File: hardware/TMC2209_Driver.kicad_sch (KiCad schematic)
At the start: 30 parts, among them J1 PCIe_Stepper, J2 Conn_01x04_Male, U1 TMC2209-LA, U2 74LVC1G06, U3 24LC02

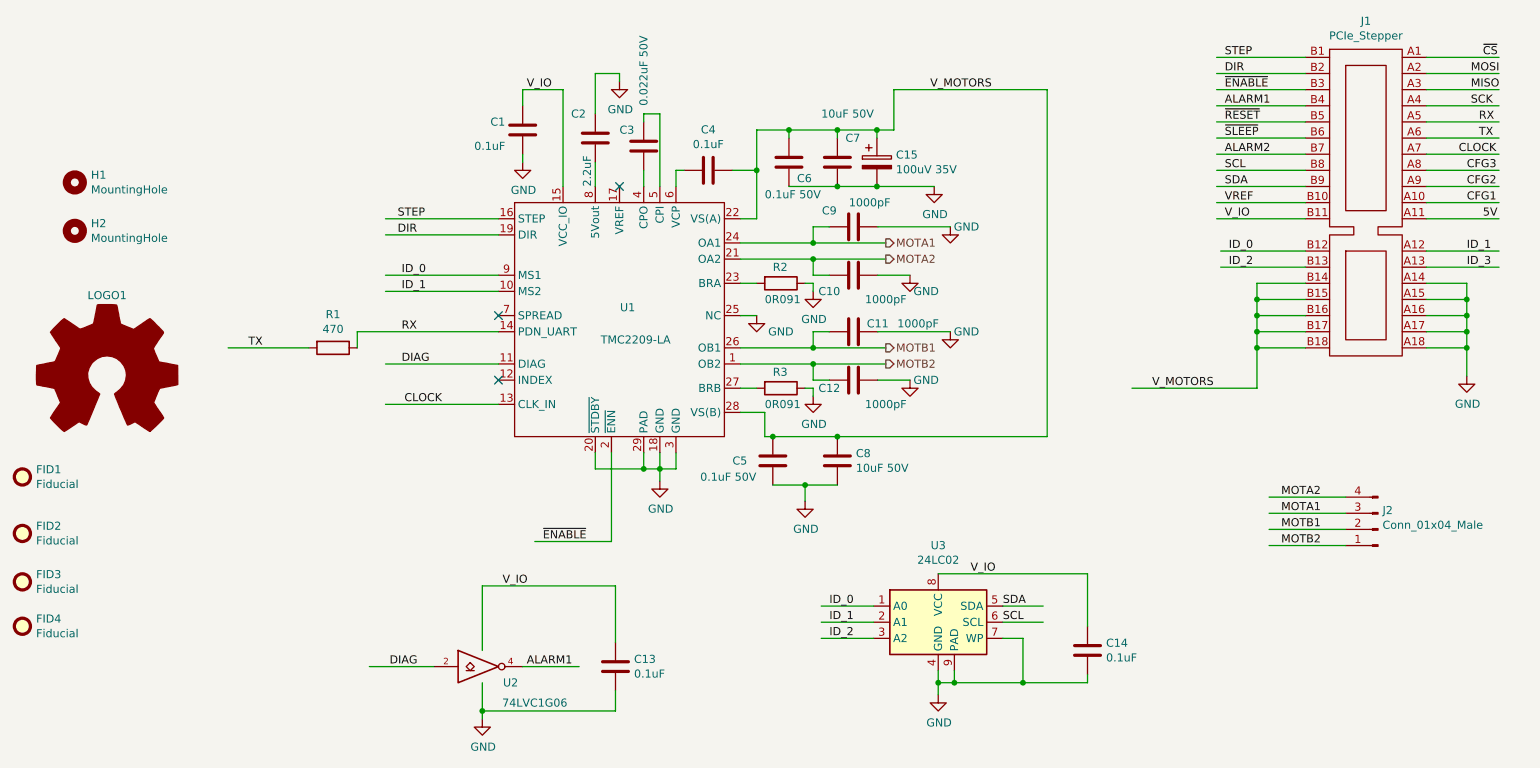
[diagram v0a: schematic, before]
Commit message: Added jumper for the TMC2209 driver clock selection.
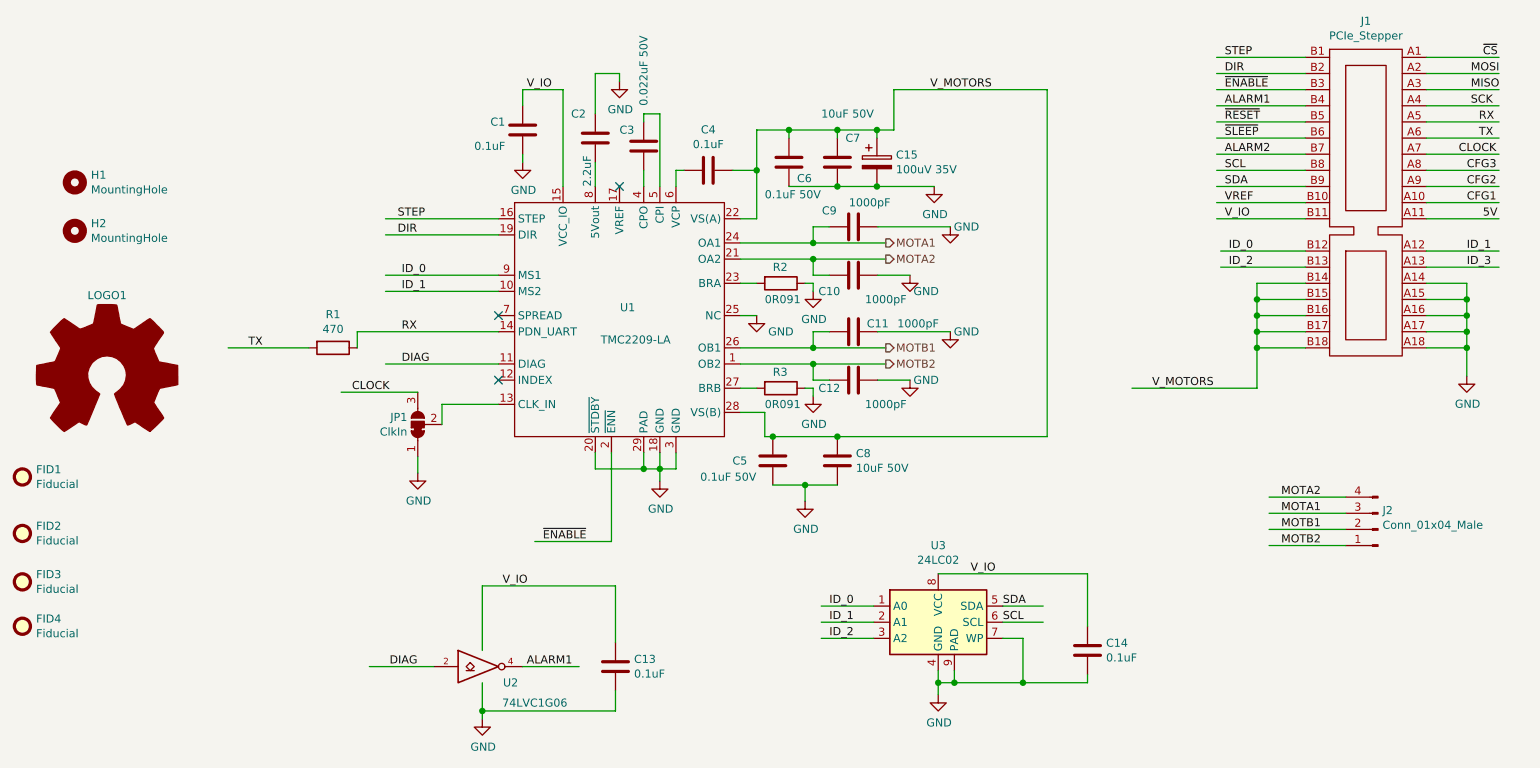
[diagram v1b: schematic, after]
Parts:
- added JP1: ClkIn, Jumper:SolderJumper-3_P1.3mm_Bridged12_Pad1.0x1.5mm, symbol Jumper:SolderJumper_3_Bridged12
- FID1, FID2, FID3, FID4, H1, H2, J1, LOGO1: now left out of the parts list
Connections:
- net CLOCK: now also JP1.3 (B); no longer U1.13 (CLK_IN)
- net GND: now also JP1.1 (A)
- new net: JP1.2 (C), U1.13 (CLK_IN)

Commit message: Convert SCH files to latest version. Fix DRC Warnings in PrntrBoard.
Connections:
- net ~CS renamed ~{CS}
- net ~ENABLE renamed ~{ENABLE}
- net ~RESET renamed ~{RESET}
- net ~SLEEP renamed ~{SLEEP}
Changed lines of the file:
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@@
-(kicad_sch (version 20201015) (generator eeschema)
+(kicad_sch (version 20210621) (generator eeschema)
   (paper "A4")
   (junction (at 99.06 151.13) (diameter 1.016) (color 0 0 0 0))
@@
   (junction (at 254 91.44) (diameter 1.016) (color 0 0 0 0))
   (junction (at 254 93.98) (diameter 1.016) (color 0 0 0 0))
+  (no_connect (at 101.6 88.9))
   (no_connect (at 101.6 99.06))
   (no_connect (at 120.65 68.58))
-  (no_connect (at 101.6 88.9))
   (wire (pts (xy 71.755 93.98) (xy 59.055 93.98))
     (stroke (width 0) (type solid) (color 0 0 0 0))
@@
     (effects (font (size 1.27 1.27)) (justify left bottom))
   )
-  (label "~ENABLE" (at 108.585 124.46 0)
+  (label "~{ENABLE}" (at 108.585 124.46 0)
     (effects (font (size 1.27 1.27)) (justify left bottom))
   )
@@
     (effects (font (size 1.27 1.27)) (justify left bottom))
   )
-  (label "~ENABLE" (at 215.9 53.34 0)
+  (label "~{ENABLE}" (at 215.9 53.34 0)
     (effects (font (size 1.27 1.27)) (justify left bottom))
   )
@@
     (effects (font (size 1.27 1.27)) (justify left bottom))
   )
-  (label "~RESET" (at 215.9 58.42 0)
-    (effects (font (size 1.27 1.27)) (justify left bottom))
-  )
-  (label "~SLEEP" (at 215.9 60.96 0)
+  (label "~{RESET}" (at 215.9 58.42 0)
+    (effects (font (size 1.27 1.27)) (justify left bottom))
+  )
+  (label "~{SLEEP}" (at 215.9 60.96 0)
     (effects (font (size 1.27 1.27)) (justify left bottom))
   )
@@
     (effects (font (size 1.27 1.27)) (justify left bottom))
   )
-  (label "~CS" (at 256.54 48.26 0)
+  (label "~{CS}" (at 256.54 48.26 0)
     (effects (font (size 1.27 1.27)) (justify left bottom))
   )
@@
       (effects (font (size 1.27 1.27)) hide)
     )
+    (pin "1")
   )
   (symbol (lib_id "power:GND") (at 99.06 152.4 0) (unit 1)
@@
       (effects (font (size 1.27 1.27)) hide)
     )
+    (pin "1")
   )
   (symbol (lib_id "power:GND") (at 105.41 64.77 0) (unit 1)
@@
       (effects (font (size 1.27 1.27)) hide)
     )
+    (pin "1")
   )
   (symbol (lib_id "power:GND") (at 120.65 52.07 0) (unit 1)
@@
       (effects (font (size 1.27 1.27)) hide)
     )
+    (pin "1")
   )
   (symbol (lib_id "power:GND") (at 127 114.935 0) (unit 1)
@@
       (effects (font (size 1.27 1.27)) hide)
     )
+    (pin "1")
   )
   (symbol (lib_id "power:GND") (at 142.24 88.9 0) (unit 1)
@@
       (effects (font (size 1.27 1.27)) hide)
     )
+    (pin "1")
   )
   (symbol (lib_id "power:GND") (at 149.86 118.11 0) (unit 1)
@@
       (effects (font (size 1.27 1.27)) hide)
     )
+    (pin "1")
   )
   (symbol (lib_id "power:GND") (at 151.13 85.09 0) (unit 1)
@@
       (effects (font (size 1.27 1.27)) hide)
     )
+    (pin "1")
   )
   (symbol (lib_id "power:GND") (at 151.13 101.6 0) (unit 1)
@@
       (effects (font (size 1.27 1.27)) hide)
     )
+    (pin "1")
   )
   (symbol (lib_id "power:GND") (at 166.37 82.55 0) (unit 1)
@@
       (effects (font (size 1.27 1.27)) hide)
     )
+    (pin "1")
   )
   (symbol (lib_id "power:GND") (at 166.37 99.06 0) (unit 1)
@@
       (effects (font (size 1.27 1.27)) hide)
     )
+    (pin "1")
   )
   (symbol (lib_id "power:GND") (at 170.18 68.58 0) (unit 1)
@@
       (effects (font (size 1.27 1.27)) hide)
     )
+    (pin "1")
   )
   (symbol (lib_id "power:GND") (at 170.815 148.59 0) (unit 1)
@@
       (effects (font (size 1.27 1.27)) hide)
     )
+    (pin "1")
   )
   (symbol (lib_id "power:GND") (at 172.72 74.93 0) (unit 1)
@@
       (effects (font (size 1.27 1.27)) hide)
     )
+    (pin "1")
   )
   (symbol (lib_id "power:GND") (at 172.72 91.44 0) (unit 1)
@@
       (effects (font (size 1.27 1.27)) hide)
     )
+    (pin "1")
   )
   (symbol (lib_id "power:GND") (at 254 98.425 0) (unit 1)
@@
       (effects (font (size 1.27 1.27)) hide)
     )
+    (pin "1")
   )
   (symbol (lib_id "Mechanical:Fiducial") (at 26.67 114.3 0) (unit 1)
@@
       (effects (font (size 1.27 1.27)) hide)
     )
+    (pin "1")
+    (pin "2")
   )
   (symbol (lib_id "Device:R") (at 146.05 83.82 270) (unit 1)
@@
       (effects (font (size 1.27 1.27)) hide)
     )
+    (pin "1")
+    (pin "2")
   )
   (symbol (lib_id "Device:R") (at 146.05 100.33 270) (unit 1)
@@
       (effects (font (size 1.27 1.27)) hide)
     )
+    (pin "1")
+    (pin "2")
   )
   (symbol (lib_id "Device:C") (at 105.41 59.69 0) (unit 1)
@@
       (effects (font (size 1.27 1.27)) hide)
     )
+    (pin "1")
+    (pin "2")
   )
   (symbol (lib_id "Device:C") (at 116.84 60.96 0) (unit 1)
@@
       (effects (font (size 1.27 1.27)) hide)
     )
+    (pin "1")
+    (pin "2")
   )
   (symbol (lib_id "Device:C") (at 120.015 144.145 0) (unit 1)
@@
       (effects (font (size 1.27 1.27)) hide)
     )
+    (pin "1")
+    (pin "2")
   )
   (symbol (lib_id "Device:C") (at 124.46 62.23 0) (unit 1)
@@
       (effects (font (size 1.27 1.27)) hide)
     )
+    (pin "1")
+    (pin "2")
   )
   (symbol (lib_id "Device:C") (at 134.62 66.04 270) (unit 1)
@@
       (effects (font (size 1.27 1.27)) hide)
     )
+    (pin "1")
+    (pin "2")
   )
   (symbol (lib_id "Device:C") (at 144.78 111.76 0) (unit 1)
@@
       (effects (font (size 1.27 1.27)) hide)
     )
+    (pin "1")
+    (pin "2")
   )
   (symbol (lib_id "Device:C") (at 147.32 64.77 0) (unit 1)
@@
       (effects (font (size 1.27 1.27)) hide)
     )
+    (pin "1")
+    (pin "2")
   )
   (symbol (lib_id "Device:C") (at 154.94 64.77 0) (unit 1)
@@
       (effects (font (size 1.27 1.27)) hide)
     )
+    (pin "1")
+    (pin "2")
   )
   (symbol (lib_id "Device:C") (at 154.94 111.76 0) (unit 1)
@@
       (effects (font (size 1.27 1.27)) hide)
     )
+    (pin "1")
+    (pin "2")
   )
   (symbol (lib_id "Device:C") (at 157.48 74.93 270) (unit 1)
@@
       (effects (font (size 1.27 1.27)) hide)
     )
+    (pin "1")
+    (pin "2")
   )
   (symbol (lib_id "Device:C") (at 157.48 82.55 270) (unit 1)
@@
       (effects (font (size 1.27 1.27)) hide)
     )
+    (pin "1")
+    (pin "2")
   )
   (symbol (lib_id "Device:C") (at 157.48 91.44 270) (unit 1)
@@
       (effects (font (size 1.27 1.27)) hide)
     )
+    (pin "1")
+    (pin "2")
   )
   (symbol (lib_id "Device:C") (at 157.48 99.06 270) (unit 1)
@@
       (effects (font (size 1.27 1.27)) hide)
     )
+    (pin "1")
+    (pin "2")
   )
   (symbol (lib_id "Device:CP") (at 161.163 64.77 0) (unit 1)
@@
       (effects (font (size 1.27 1.27)) hide)
     )
+    (pin "1")
+    (pin "2")
   )
   (symbol (lib_id "Device:C") (at 194.31 141.605 0) (unit 1)
@@
       (effects (font (size 1.27 1.27)) hide)
     )
+    (pin "1")
+    (pin "2")
   )
   (symbol (lib_id "Connector:Conn_01x04_Male") (at 240.03 122.555 180) (unit 1)
@@
       (effects (font (size 1.27 1.27)) hide)
     )
+    (pin "1")
+    (pin "2")
+    (pin "3")
+    (pin "4")
   )
   (symbol (lib_id "Jumper:SolderJumper_3_Bridged12") (at 88.9 106.045 90) (unit 1)
@@
       (effects (font (size 1.27 1.27)) hide)
     )
+    (pin "1")
+    (pin "2")
+    (pin "3")
   )
   (symbol (lib_id "Logic_74xgxx:74LVC1G06") (at 99.06 144.145 0) (unit 1)
@@
       (effects (font (size 1.27 1.27)) hide)
     )
+    (pin "2")
+    (pin "3")
+    (pin "4")
+    (pin "5")
   )
   (symbol (lib_id "24lc02:24LC02") (at 170.815 137.16 0) (unit 1)
@@
       (effects (font (size 1.27 1.27)) hide)
     )
+    (pin "1")
+    (pin "2")
+    (pin "3")
+    (pin "4")
+    (pin "5")
+    (pin "6")
+    (pin "7")
+    (pin "8")
+    (pin "9")
   )
   (symbol (lib_id "Graphic:Logo_Open_Hardware_Large") (at 40.005 98.425 0) (unit 1)
@@
       (effects (font (size 1.27 1.27)) hide)
     )
+    (pin "A1")
+    (pin "A10")
+    (pin "A11")
+    (pin "A12")
+    (pin "A13")
+    (pin "A14")
+    (pin "A15")
+    (pin "A16")
+    (pin "A17")
+    (pin "A18")
+    (pin "A2")
+    (pin "A3")
+    (pin "A4")
+    (pin "A5")
+    (pin "A6")
+    (pin "A7")
+    (pin "A8")
+    (pin "A9")
+    (pin "B1")
+    (pin "B10")
+    (pin "B11")
+    (pin "B12")
+    (pin "B13")
+    (pin "B14")
+    (pin "B15")
+    (pin "B16")
+    (pin "B17")
+    (pin "B18")
+    (pin "B2")
+    (pin "B3")
+    (pin "B4")
+    (pin "B5")
+    (pin "B6")
+    (pin "B7")
+    (pin "B8")
+    (pin "B9")
   )
   (symbol (lib_id "tmc2209:TMC2209-LA") (at 120.65 90.17 0) (unit 1)
@@
       (effects (font (size 1.27 1.27)) hide)
     )
+    (pin "1")
+    (pin "10")
+    (pin "11")
+    (pin "12")
+    (pin "13")
+    (pin "14")
+    (pin "15")
+    (pin "16")
+    (pin "17")
+    (pin "18")
+    (pin "19")
+    (pin "2")
+    (pin "20")
+    (pin "21")
+    (pin "22")
+    (pin "23")
+    (pin "24")
+    (pin "25")
+    (pin "26")
+    (pin "27")
+    (pin "28")
+    (pin "29")
+    (pin "3")
+    (pin "4")
+    (pin "5")
+    (pin "6")
+    (pin "7")
+    (pin "8")
+    (pin "9")
   )
   (sheet_instances

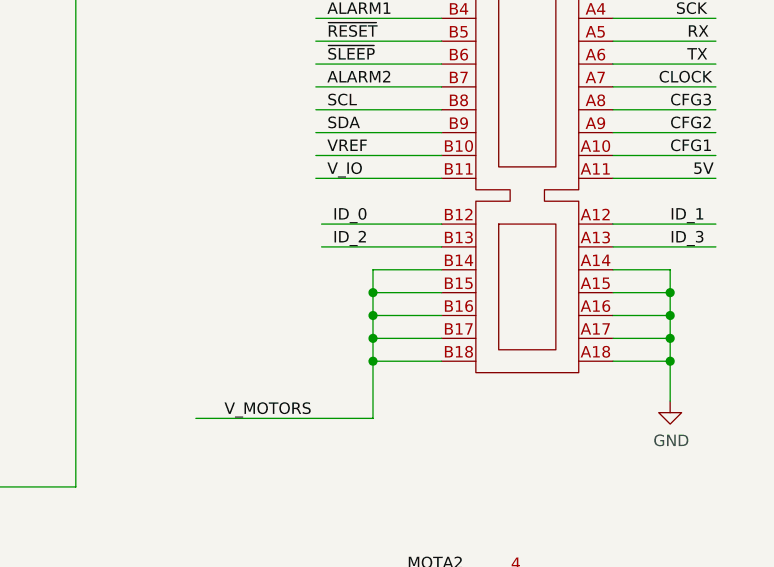
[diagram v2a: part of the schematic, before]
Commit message: Update drivers to respect high motor coltage circuit.
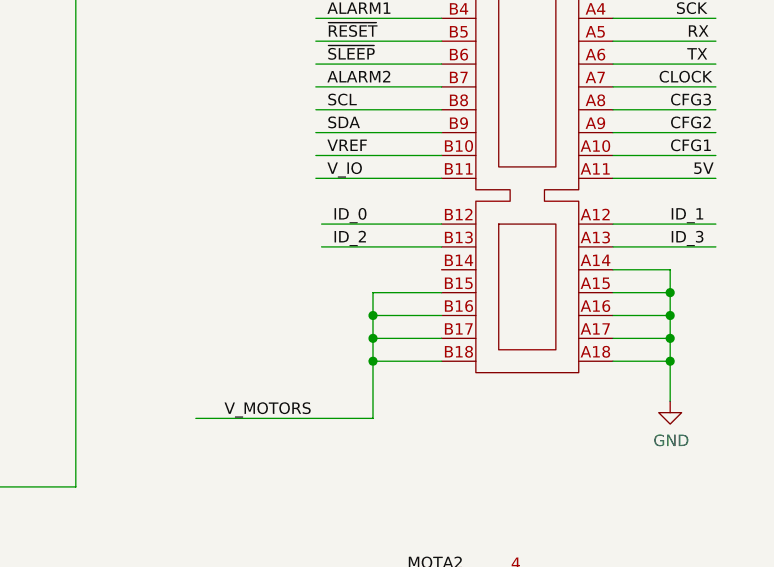
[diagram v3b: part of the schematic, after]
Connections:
- net V_MOTORS: no longer J1.B14
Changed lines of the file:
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@@
   (junction (at 173.355 146.685) (diameter 1.016) (color 0 0 0 0))
   (junction (at 184.15 146.685) (diameter 1.016) (color 0 0 0 0))
-  (junction (at 220.98 86.36) (diameter 1.016) (color 0 0 0 0))
   (junction (at 220.98 88.9) (diameter 1.016) (color 0 0 0 0))
   (junction (at 220.98 91.44) (diameter 1.016) (color 0 0 0 0))
@@
     (stroke (width 0) (type solid) (color 0 0 0 0))
   )
-  (wire (pts (xy 220.98 83.82) (xy 220.98 86.36))
-    (stroke (width 0) (type solid) (color 0 0 0 0))
-  )
   (wire (pts (xy 220.98 86.36) (xy 220.98 88.9))
     (stroke (width 0) (type solid) (color 0 0 0 0))
@@
     (stroke (width 0) (type solid) (color 0 0 0 0))
   )
-  (wire (pts (xy 228.6 83.82) (xy 220.98 83.82))
-    (stroke (width 0) (type solid) (color 0 0 0 0))
-  )
